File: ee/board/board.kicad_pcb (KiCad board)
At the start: 4 copper layers, 87.1 x 51 mm, 55 parts, among them J1 Lichee_RV_J3, J2 Lichee_RV_J4, J3 USB_A, J4 Conn_01x08_Pin, J5 Conn_01x10_Pin, J6 Conn_Coaxial, J8 HR911105A, U1 RTL8201F, U2 RTL8723DS, U6 USBLC6-2SC6, Y1 Crystal_GND24_Small

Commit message: Nearly finished routing.
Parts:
- removed RN3, RN4: 10k, Resistor_SMD:R_Array_Convex_4x0402
- added C16: 100nF, Capacitor_SMD:C_0603_1608Metric, F.Cu at (168.4, 118.5)
- added L2: 120R@100MHz, Inductor_SMD:L_0805_2012Metric, F.Cu at (138.7, 117.0)
- added R10: 5.1k, Resistor_SMD:R_0603_1608Metric, F.Cu at (173.2, 126.8)
- added R11: 5.1k, Resistor_SMD:R_0603_1608Metric, F.Cu at (165.5, 120.8)
- added R5: 5.1k, Resistor_SMD:R_0603_1608Metric, F.Cu at (164.0, 120.8)
- added R6: 5.1k, Resistor_SMD:R_0603_1608Metric, F.Cu at (167.0, 120.8)
- added R7: 5.1k, Resistor_SMD:R_0603_1608Metric, F.Cu at (176.2, 125.4)
- added R8: 5.1k, Resistor_SMD:R_0603_1608Metric, F.Cu at (168.4, 117.0)
- added R9: 5.1k, Resistor_SMD:R_0603_1608Metric, F.Cu at (173.2, 128.4)
- JP2, JP3: moved to B.Cu
- moved RN7 91.3 mm to (120.5, 136.2), turned to -90 degrees
- moved RN6 85.9 mm to (123.2, 136.2), turned to -90 degrees
- moved RN5 80.6 mm to (125.7, 136.2), turned to -90 degrees
- moved R31 70.7 mm to (159.6, 99.2), turned to -90 degrees
- moved R33 70.5 mm to (159.6, 102.2), turned to -90 degrees
- moved R32 69.2 mm to (161.2, 102.2), turned to 90 degrees
- moved R34 68.7 mm to (161.2, 99.2), turned to -90 degrees
- moved R15 65.3 mm to (157.9, 120.8), turned to -90 degrees
- moved R13 65.2 mm to (150.8, 123.6), turned to 180 degrees
- moved C18 62.2 mm to (161.2, 110.4), turned to -90 degrees
- moved R14 60.8 mm to (153.9, 123.6), turned to 180 degrees
- moved C8 60.7 mm to (166.2, 123.6), turned to 180 degrees
- moved R30 59.6 mm to (172.2, 130.0), turned to 180 degrees
- moved C9 59.4 mm to (172.2, 132.2)
- moved RN1 56.3 mm to (142.0, 115.6), turned to 180 degrees
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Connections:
- J1 pad 45: /RMII_TXCK -> Net-(J1-PE3)
- RN5 pad 1: Net-(J1-PE4) -> Net-(J1-PE0)
- RN5 pad 2: Net-(J1-PE1) -> Net-(J1-PE2)
- RN5 pad 3: Net-(J1-PE2) -> Net-(J1-PE1)
- RN5 pad 4: Net-(J1-PE0) -> Net-(J1-PE3)
- RN5 pad 5: /Ethernet/RMII_CRS_DV -> /Ethernet/RMII_TXCK
- RN5 pad 6: /Ethernet/RMII_RXD1 -> /Ethernet/RMII_RXD0
- RN5 pad 7: /Ethernet/RMII_RXD0 -> /Ethernet/RMII_RXD1
- RN5 pad 8: /Ethernet/RMII_TXD0 -> /Ethernet/RMII_CRS_DV
- RN6 pad 1: Net-(J1-PE8) -> Net-(J1-PE4)
- RN6 pad 2: Net-(J1-PE6) -> Net-(J1-PE5)
- RN6 pad 4: Net-(J1-PE5) -> Net-(J1-PE6)
- RN6 pad 5: /Ethernet/RMII_TXD1 -> /Ethernet/RMII_TXEN
- RN6 pad 7: /Ethernet/RMII_TXEN -> /Ethernet/RMII_TXD1
- RN6 pad 8: /Ethernet/RMII_MDC -> /Ethernet/RMII_TXD0
- RN7 pad 1: unconnected-(RN7-R1.1-Pad1) -> Net-(J1-PE8)
- RN7 pad 2: Net-(J1-PE16) -> Net-(J1-PE9)
- RN7 pad 3: /RMII_TXCK -> Net-(J1-PE16)
- RN7 pad 4: Net-(J1-PE9) -> unconnected-(RN7-R4.1-Pad4)
- RN7 pad 5: /Ethernet/RMII_MDIO -> unconnected-(RN7-R4.2-Pad5)
- RN7 pad 6: /Ethernet/RMII_TXCK -> /Ethernet/RST
- RN7 pad 7: /Ethernet/RST -> /Ethernet/RMII_MDIO
- RN7 pad 8: unconnected-(RN7-R1.2-Pad8) -> /Ethernet/RMII_MDC
- U6 pad 1: Net-(R2-Pad1) -> Net-(R1-Pad1)
- U6 pad 3: Net-(R1-Pad1) -> Net-(R2-Pad1)
- U6 pad 4: Net-(J3-D+) -> Net-(J3-D-)
- U6 pad 6: Net-(J3-D-) -> Net-(J3-D+)
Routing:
- net +5V: track 0.00 -> 100.9 mm, vias 0 -> 2
- net /Ethernet/RMII_RXER: track 0.00 -> 67.9 mm, vias 0 -> 2
- net /Ethernet/RMII_MDIO: track 0.00 -> 66.8 mm
- net /Ethernet/RMII_RXD1: track 0.00 -> 65.6 mm
- net /Ethernet/RMII_RXD0: track 0.00 -> 65.1 mm
- net /Ethernet/RST: track 0.00 -> 64.7 mm
- net /Ethernet/RMII_MDC: track 0.00 -> 64.6 mm
- net /Ethernet/RMII_TXEN: track 0.00 -> 61.1 mm
- net /Ethernet/RMII_CRS_DV: track 0.00 -> 59.9 mm, vias 0 -> 2
- net /Ethernet/RMII_TXD1: track 0.00 -> 58.9 mm
- net /Ethernet/RMII_TXD0: track 0.00 -> 58.7 mm
- net /Ethernet/RMII_TXCK: track 0.00 -> 58.1 mm
- net /USB_HOST_N: track 0.00 -> 44.1 mm
- net /USB_HOST_P: track 0.00 -> 40.5 mm
- net /Ethernet/LED1: track 0.00 -> 32.0 mm, vias 0 -> 2
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- added copper zone on In2.Cu, net +3.3VA
- added copper zone on In2.Cu, net +3V3
- removed copper zone on In2.Cu, net GND
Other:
- board size 87.1 x 51 mm -> 87.1 x 53.4 mm

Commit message: Finished R1
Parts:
- added SW1: SW_Push, Button_Switch_SMD:SW_SPST_PTS645, F.Cu at (134.8, 97.4)
- moved C7 0.14 mm to (154.2, 101.3)
- moved C6 0.10 mm to (154.2, 106.0)
- moved R3 0.08 mm to (153.5, 103.7)
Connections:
- J1 pad 76: (no net) -> GND
- J1 pad 77: (no net) -> GND
- J2 pad 76: (no net) -> GND
- J2 pad 77: (no net) -> GND
- J8 pad 13: (no net) -> GND
- J8 pad 14: (no net) -> GND
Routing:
- net Net-(R19-Pad2): track 0.00 -> 68.8 mm, vias 0 -> 2
- net Net-(J6-In): track 0.00 -> 13.0 mm
- net Net-(C13-Pad1): track 13.2 -> 5.76 mm, vias 0 -> 1
- net Net-(U2-WIFI/BT_ANT): track 0.00 -> 4.66 mm

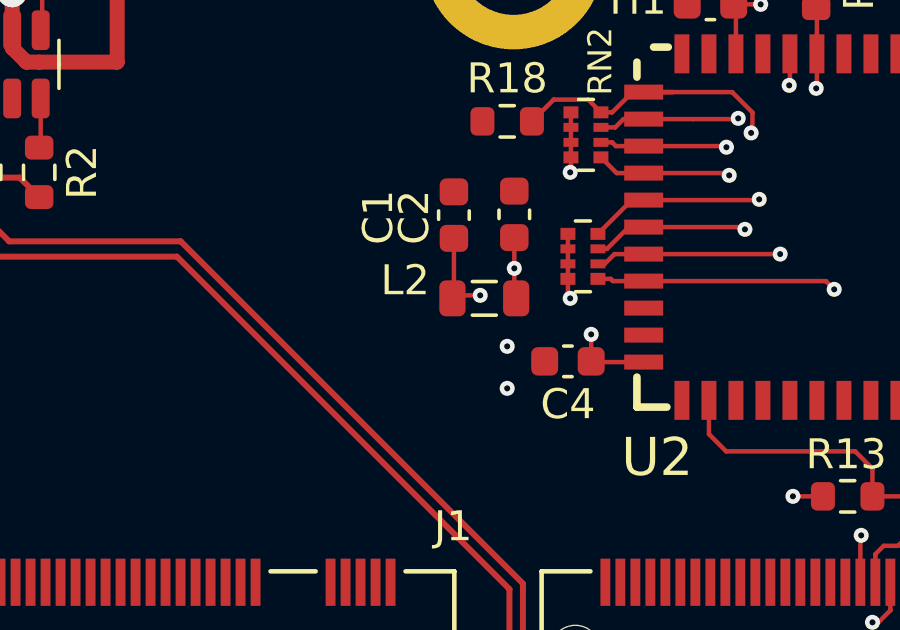
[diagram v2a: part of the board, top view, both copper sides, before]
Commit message: Changed inductor side in R0.1 to fit the part number.
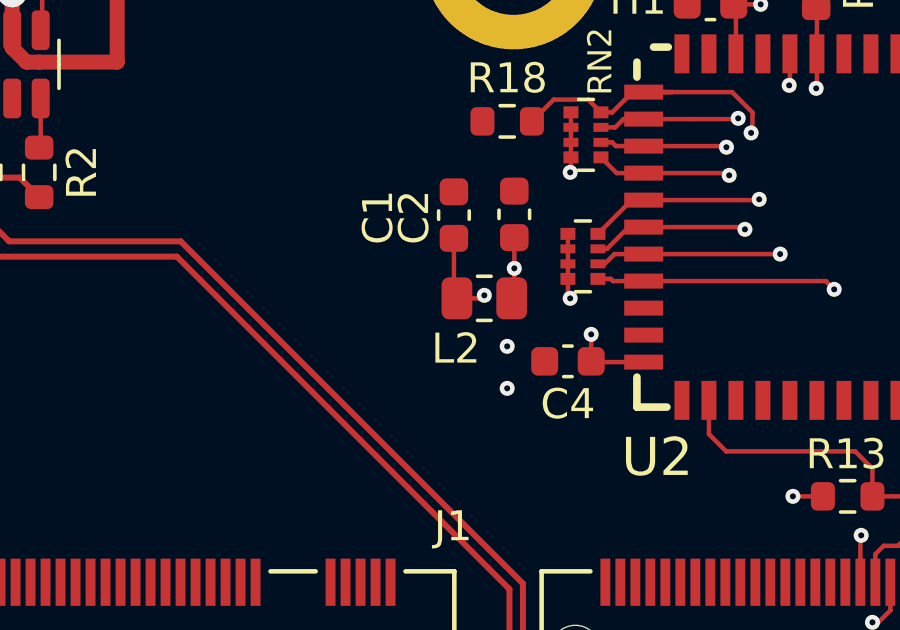
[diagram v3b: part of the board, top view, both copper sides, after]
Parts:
- L2: footprint Inductor_SMD:L_0805_2012Metric -> Resistor_SMD:R_0805_2012Metric

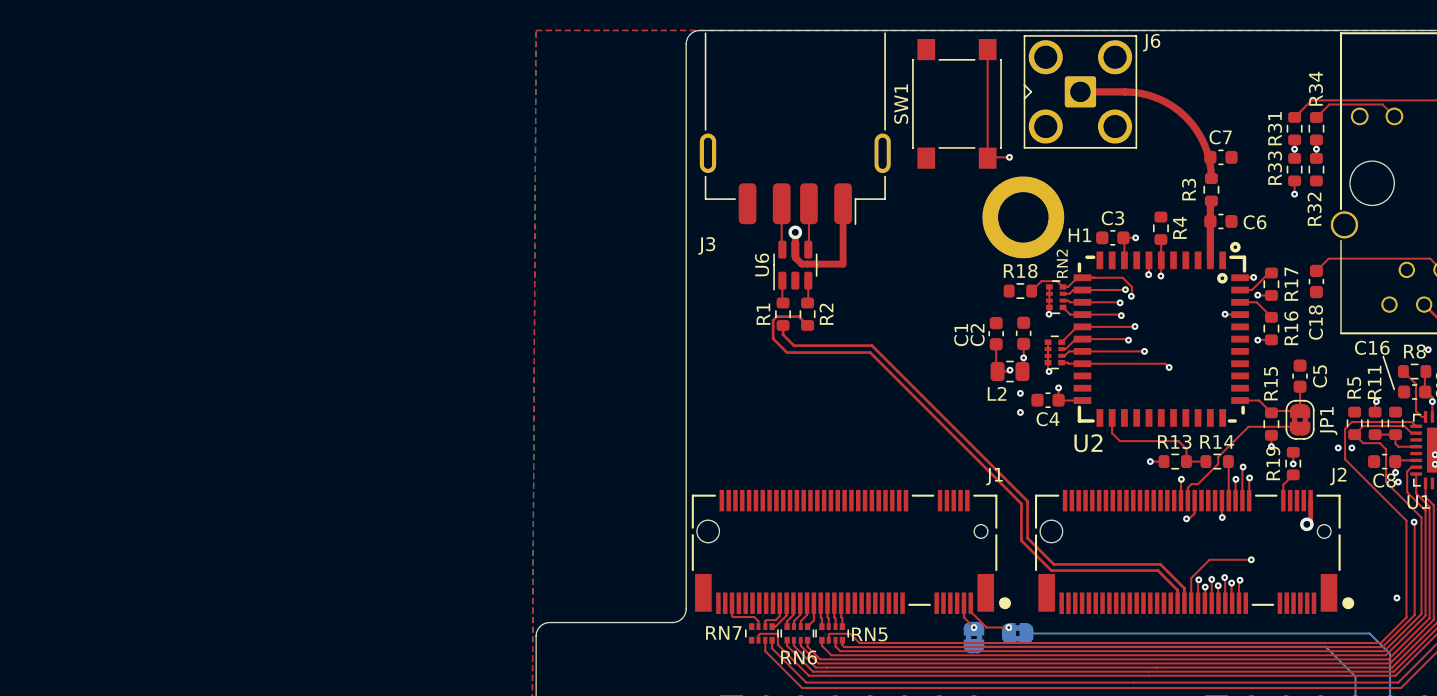
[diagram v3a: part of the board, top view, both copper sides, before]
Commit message: Moved to a chip scale
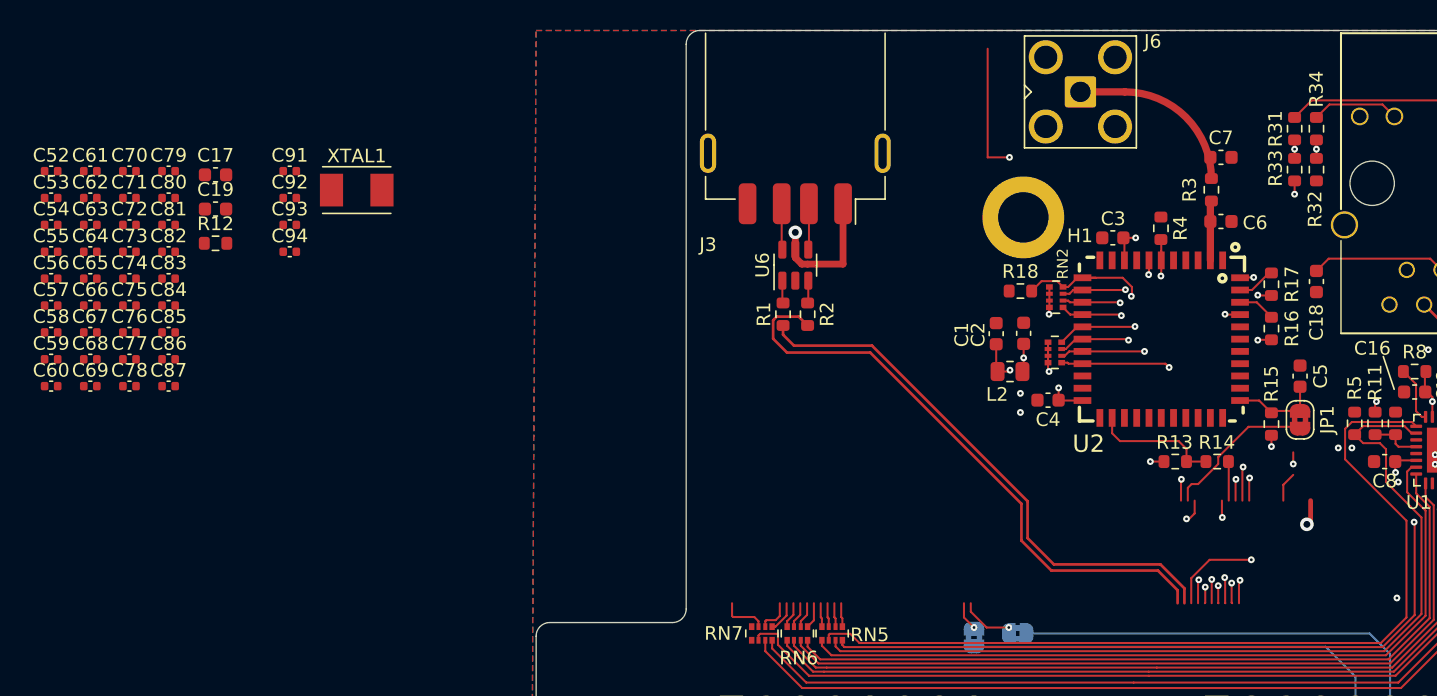
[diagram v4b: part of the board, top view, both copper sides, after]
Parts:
- removed J1: Lichee_RV_J3, KiLib:CONN75_2199230-3
- removed J2: Lichee_RV_J4, KiLib:CONN75_2199230-3
- removed R19: 100R, Resistor_SMD:R_0603_1608Metric
- removed SW1: SW_Push, Button_Switch_SMD:SW_SPST_PTS645
- added C17: 5PF 50V C0G/NP0 0603, Capacitor_SMD:C_0603_1608Metric, F.Cu at (80.5, 102.6)
- added C19: 5PF 50V C0G/NP0 0603, Capacitor_SMD:C_0603_1608Metric, F.Cu at (80.5, 105.1)
- added C52: 16V 0.1uF X7R 0402, Capacitor_SMD:C_0402_1005Metric, F.Cu at (68.5, 102.3)
- added C53: 16V 0.1uF X7R 0402, Capacitor_SMD:C_0402_1005Metric, F.Cu at (68.5, 104.3)
- added C54: 16V 0.1uF X7R 0402, Capacitor_SMD:C_0402_1005Metric, F.Cu at (68.5, 106.2)
- added C55: 16V 0.1uF X7R 0402, Capacitor_SMD:C_0402_1005Metric, F.Cu at (68.5, 108.2)
- added C56: 16V 0.1uF X7R 0402, Capacitor_SMD:C_0402_1005Metric, F.Cu at (68.5, 110.2)
- added C57: 16V 0.1uF X7R 0402, Capacitor_SMD:C_0402_1005Metric, F.Cu at (68.5, 112.2)
- added C58: 16V 0.1uF X7R 0402, Capacitor_SMD:C_0402_1005Metric, F.Cu at (68.5, 114.1)
- added C59: 16V 0.1uF X7R 0402, Capacitor_SMD:C_0402_1005Metric, F.Cu at (68.5, 116.1)
- added C60: 16V 0.1uF X7R 0402, Capacitor_SMD:C_0402_1005Metric, F.Cu at (68.5, 118.1)
- added C61: 16V 0.1uF X7R 0402, Capacitor_SMD:C_0402_1005Metric, F.Cu at (71.3, 102.3)
- added C62: 16V 0.1uF X7R 0402, Capacitor_SMD:C_0402_1005Metric, F.Cu at (71.3, 104.3)
- added C63: 16V 0.1uF X7R 0402, Capacitor_SMD:C_0402_1005Metric, F.Cu at (71.3, 106.2)
- added C64: 16V 0.1uF X7R 0402, Capacitor_SMD:C_0402_1005Metric, F.Cu at (71.3, 108.2)
- added C65: 16V 0.1uF X7R 0402, Capacitor_SMD:C_0402_1005Metric, F.Cu at (71.3, 110.2)
- added C66: 16V 0.1uF X7R 0402, Capacitor_SMD:C_0402_1005Metric, F.Cu at (71.3, 112.2)
- added C67: 16V 0.1uF X7R 0402, Capacitor_SMD:C_0402_1005Metric, F.Cu at (71.3, 114.1)
- added C68: 16V 0.1uF X7R 0402, Capacitor_SMD:C_0402_1005Metric, F.Cu at (71.3, 116.1)
- added C69: 16V 0.1uF X7R 0402, Capacitor_SMD:C_0402_1005Metric, F.Cu at (71.3, 118.1)
- added C70: 4.7 uF 16V 0805 X7R, Capacitor_SMD:C_0402_1005Metric, F.Cu at (74.2, 102.3)
- added C71: 4.7 uF 16V 0805 X7R, Capacitor_SMD:C_0402_1005Metric, F.Cu at (74.2, 104.3)
- added C72: 4.7 uF 16V 0805 X7R, Capacitor_SMD:C_0402_1005Metric, F.Cu at (74.2, 106.2)
- added C73: 4.7 uF 16V 0805 X7R, Capacitor_SMD:C_0402_1005Metric, F.Cu at (74.2, 108.2)
- added C74: 4.7 uF 16V 0805 X7R, Capacitor_SMD:C_0402_1005Metric, F.Cu at (74.2, 110.2)
- added C75: 4.7 uF 16V 0805 X7R, Capacitor_SMD:C_0402_1005Metric, F.Cu at (74.2, 112.2)
- added C76: 4.7 uF 16V 0805 X7R, Capacitor_SMD:C_0402_1005Metric, F.Cu at (74.2, 114.1)
- added C77: 4.7 uF 16V 0805 X7R, Capacitor_SMD:C_0402_1005Metric, F.Cu at (74.2, 116.1)
- added C78: 4.7 uF 16V 0805 X7R, Capacitor_SMD:C_0402_1005Metric, F.Cu at (74.2, 118.1)
- added C79: 4.7 uF 16V 0805 X7R, Capacitor_SMD:C_0402_1005Metric, F.Cu at (77.1, 102.3)
- added C80: 4.7 uF 16V 0805 X7R, Capacitor_SMD:C_0402_1005Metric, F.Cu at (77.1, 104.3)
- added C81: 4.7 uF 16V 0805 X7R, Capacitor_SMD:C_0402_1005Metric, F.Cu at (77.1, 106.2)
- added C82: 4.7 uF 16V 0805 X7R, Capacitor_SMD:C_0402_1005Metric, F.Cu at (77.1, 108.2)
- added C83: 4.7 uF 16V 0805 X7R, Capacitor_SMD:C_0402_1005Metric, F.Cu at (77.1, 110.2)
- added C84: 4.7 uF 16V 0805 X7R, Capacitor_SMD:C_0402_1005Metric, F.Cu at (77.1, 112.2)
- added C85: 4.7 uF 16V 0805 X7R, Capacitor_SMD:C_0402_1005Metric, F.Cu at (77.1, 114.1)
- added C86: 4.7 uF 16V 0805 X7R, Capacitor_SMD:C_0402_1005Metric, F.Cu at (77.1, 116.1)
- added C87: 4.7 uF 16V 0805 X7R, Capacitor_SMD:C_0402_1005Metric, F.Cu at (77.1, 118.1)
- added C91: 7PF 50V C0G/NP0 0603, Capacitor_SMD:C_0402_1005Metric, F.Cu at (85.9, 102.3)
- added C92: 7PF 50V C0G/NP0 0603, Capacitor_SMD:C_0402_1005Metric, F.Cu at (85.9, 104.3)
- added C93: 12PF 50V C0G/NP0, Capacitor_SMD:C_0402_1005Metric, F.Cu at (85.9, 106.2)
- added C94: 12PF 50V C0G/NP0, Capacitor_SMD:C_0402_1005Metric, F.Cu at (85.9, 108.2)
- added R12: 240R, Resistor_SMD:R_0603_1608Metric, F.Cu at (80.5, 107.6)
- added XTAL1: SC32S-7PF20PPM, Crystal:Crystal_SMD_TXC_7A-2Pin_5x3.2mm, F.Cu at (90.8, 103.7)
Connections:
- net /A4 renamed /MPU/A4
- net /A6 renamed /MPU/A6
- net /A7 renamed /MPU/A7
- net /LPO renamed /WiFi/LPO
- net /PG0_SDIO1_CLK renamed /MPU/PG0
- net /PG16_AP_WAKE_BT renamed /MPU/PG16
- net /PG1_SDIO1_CMD renamed /MPU/PG1
- net /PG2_SDIO1_D0 renamed /MPU/PG2
- net /PG3_SDIO1_D1 renamed /MPU/PG3
- net /PG4_SDIO1_D2 renamed /MPU/PG4
- net /PG5_SDIO1_D3 renamed /MPU/PG5
- JP1 pad 2: /PG18_BT_RESETN -> /MPU/PG18
- JP2 pad 1: Net-(J1-PB8) -> unconnected-(JP2-A-Pad1)
- JP3 pad 1: Net-(J1-PB9) -> unconnected-(JP3-A-Pad1)
- R14 pad 1: /PG11_CLK_FANOUT -> /MPU/PG11
- R16 pad 1: /PG7_AP_UART1_RX -> /MPU/PG7
- R17 pad 1: /PG6_AP_UART1_TX -> /MPU/PG6
- R18 pad 2: /PG12_WL_REG_ON -> /MPU/PG12
- RN2 pad 3: /PG10_WL_WAKE_AP -> /MPU/PG12
- RN2 pad 4: /PG12_WL_REG_ON -> /MPU/PG12
- RN5 pad 1: Net-(J1-PE0) -> /MPU/PE0
- RN5 pad 2: Net-(J1-PE2) -> /MPU/PE2
- RN5 pad 3: Net-(J1-PE1) -> /MPU/PE1
- RN5 pad 4: Net-(J1-PE3) -> /MPU/PE3
- RN6 pad 1: Net-(J1-PE4) -> /MPU/PE4
- RN6 pad 2: Net-(J1-PE5) -> /MPU/PE5
- RN6 pad 3: Net-(J1-PE7) -> /MPU/PE7
- RN6 pad 4: Net-(J1-PE6) -> /MPU/PE6
- RN7 pad 1: Net-(J1-PE8) -> /MPU/PE8
- RN7 pad 2: Net-(J1-PE9) -> /MPU/PE9
- RN7 pad 3: Net-(J1-PE16) -> /MPU/PE16
- U2 pad 12: /PG12_WL_REG_ON -> /MPU/PG12
- U2 pad 13: /PG10_WL_WAKE_AP -> /MPU/PG12
- U2 pad 41: /PG9_AP_UART1_CTS -> /MPU/PG9
- U2 pad 44: /PG8_AP_UART1_RTS -> /MPU/PG8
- U2 pad 7: /PG17_BT_WAKE_AP -> /MPU/PG17
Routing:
- net (no net): track 0.00 -> 71.0 mm, vias 0 -> 2
- net Net-(R19-Pad2): track 68.8 -> 0.00 mm, vias 2 -> 0
- net /MPU/PG12: track 0.00 -> 53.5 mm, vias 0 -> 4
- net /PG12_WL_REG_ON: track 29.6 -> 0.00 mm, vias 2 -> 0
- net /PG6_AP_UART1_TX: track 27.8 -> 0.00 mm, vias 2 -> 0
- net /MPU/PG6: track 0.00 -> 27.8 mm, vias 0 -> 2
- net /PG17_BT_WAKE_AP: track 24.9 -> 0.00 mm, vias 2 -> 0
- net /MPU/PG17: track 0.00 -> 24.9 mm, vias 0 -> 2
- net /PG10_WL_WAKE_AP: track 23.9 -> 0.00 mm, vias 2 -> 0
- net /PG7_AP_UART1_RX: track 21.1 -> 0.00 mm, vias 2 -> 0
- net /MPU/PG7: track 0.00 -> 21.1 mm, vias 0 -> 2
- net /PG8_AP_UART1_RTS: track 17.7 -> 0.00 mm, vias 2 -> 0
- net /MPU/PG8: track 0.00 -> 17.7 mm, vias 0 -> 2
- net /PG9_AP_UART1_CTS: track 15.5 -> 0.00 mm, vias 2 -> 0
- net /MPU/PG9: track 0.00 -> 15.5 mm, vias 0 -> 2
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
